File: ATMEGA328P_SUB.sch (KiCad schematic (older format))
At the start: 38 parts, among them J10 4/MISO, J11 5/SCK, J12 0, J13 1, J14 2, J15 ICSP1, J16 3, J17 4/SDA, J18 5/SCL, J19 0/RXD, J20 1/TXD, J21 2/INT0, J22 3/INT1, J23 4, J24 5, J25 6, J26 7, J27 5V, J28 3V3, J29 GND, J30 Vin, J4 AREF, J5 0, J6 1, J7 2, J8 7RO, J9 3/MOSI, SW1 RES, U6 ATmega328P-MU, Y2 16MHz

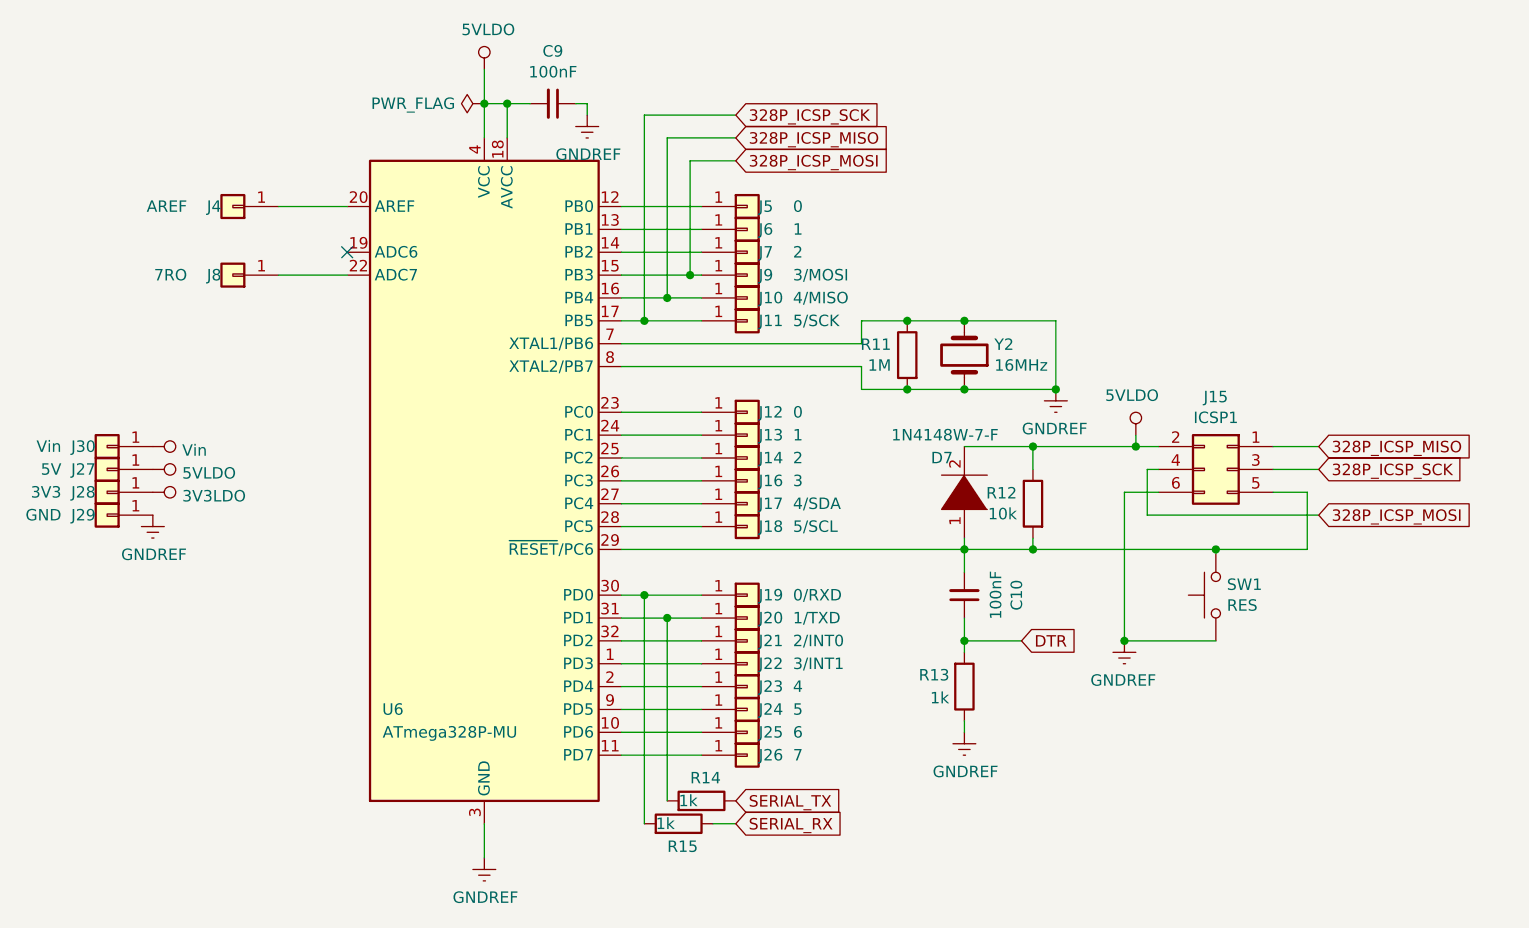
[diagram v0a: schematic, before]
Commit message: Set component footprints, added datasheets, fixed the last DRC error and a couple component values
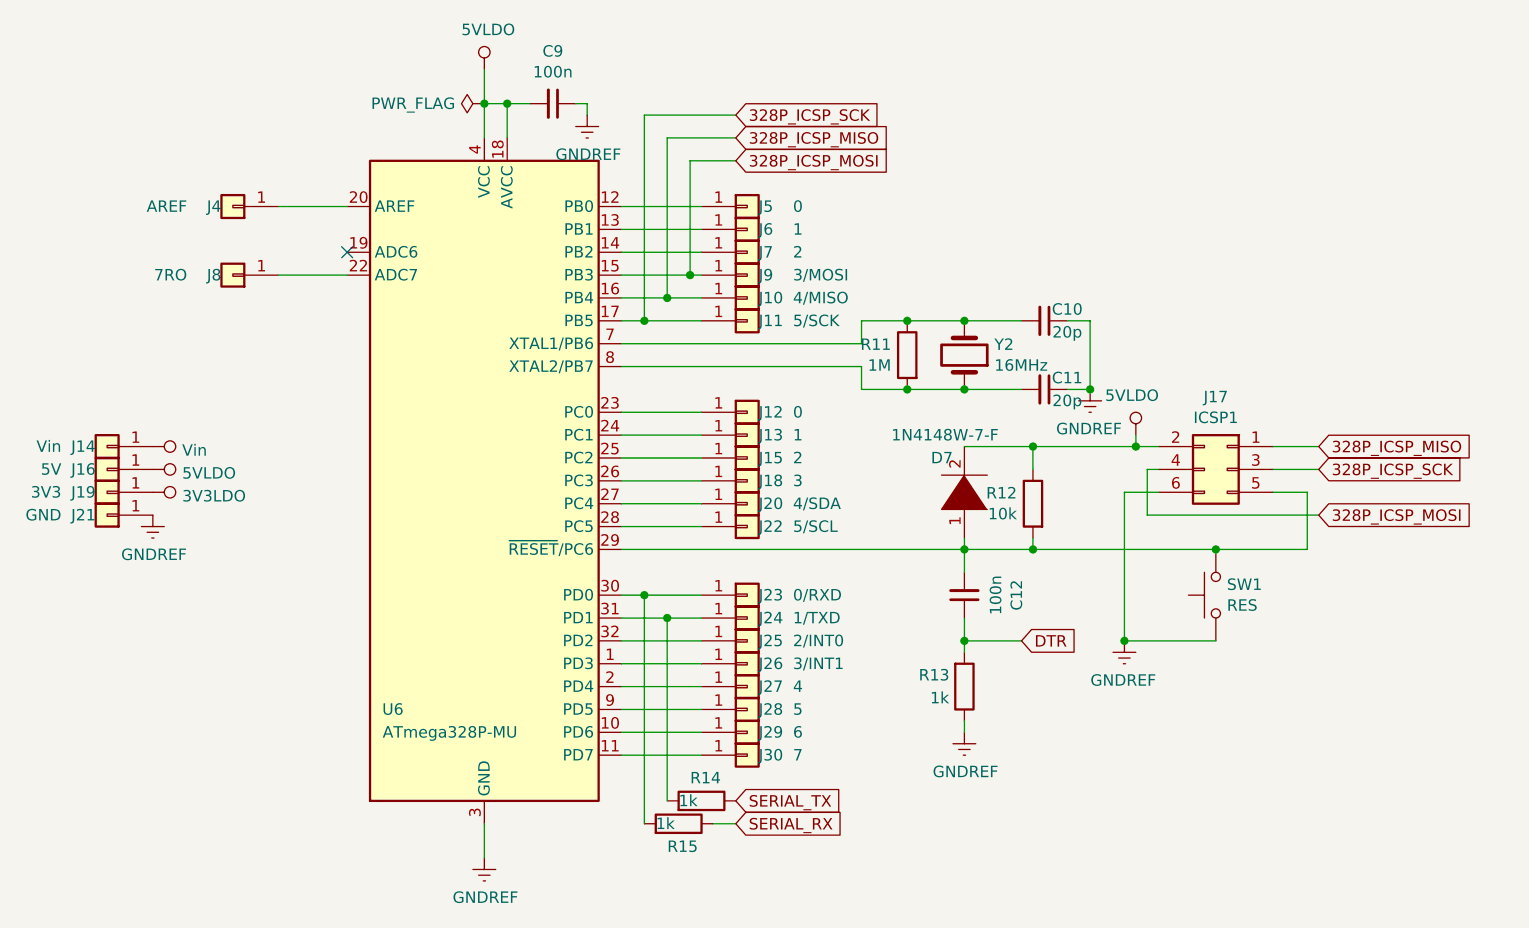
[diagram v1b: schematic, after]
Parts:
- added C10, C11: 20p, Capacitor_SMD:C_0603_1608Metric, symbol Device:C_Small
- C12: renamed from C10; value 100nF -> 100n; footprint (none) -> Capacitor_SMD:C_0603_1608Metric
- C9: value 100nF -> 100n; footprint (none) -> Capacitor_SMD:C_0603_1608Metric
- D7: footprint (none) -> Diode_SMD:D_SOD-123
- J10, J11, J12, J13, J4, J5, J6, J7, J8, J9: footprint (none) -> Connector_Pin:Pin_D1.0mm_L10.0mm
- J14: renamed from J30; footprint (none) -> Connector_Pin:Pin_D1.0mm_L10.0mm
- J15: renamed from J14; footprint (none) -> Connector_Pin:Pin_D1.0mm_L10.0mm
- J16: renamed from J27; footprint (none) -> Connector_Pin:Pin_D1.0mm_L10.0mm
- J17: renamed from J15; footprint (none) -> Connector_PinHeader_2.54mm:PinHeader_2x03_P2.54mm_Vertical
- J18: renamed from J16; footprint (none) -> Connector_Pin:Pin_D1.0mm_L10.0mm
- J19: renamed from J28; footprint (none) -> Connector_Pin:Pin_D1.0mm_L10.0mm
- J20: renamed from J17; footprint (none) -> Connector_Pin:Pin_D1.0mm_L10.0mm
- J21: renamed from J29; footprint (none) -> Connector_Pin:Pin_D1.0mm_L10.0mm
- J22: renamed from J18; footprint (none) -> Connector_Pin:Pin_D1.0mm_L10.0mm
- J23: renamed from J19; footprint (none) -> Connector_Pin:Pin_D1.0mm_L10.0mm
- J24: renamed from J20; footprint (none) -> Connector_Pin:Pin_D1.0mm_L10.0mm
- J25: renamed from J21; footprint (none) -> Connector_Pin:Pin_D1.0mm_L10.0mm
- J26: renamed from J22; footprint (none) -> Connector_Pin:Pin_D1.0mm_L10.0mm
- J27: renamed from J23; footprint (none) -> Connector_Pin:Pin_D1.0mm_L10.0mm
- J28: renamed from J24; footprint (none) -> Connector_Pin:Pin_D1.0mm_L10.0mm
- J29: renamed from J25; footprint (none) -> Connector_Pin:Pin_D1.0mm_L10.0mm
- J30: renamed from J26; footprint (none) -> Connector_Pin:Pin_D1.0mm_L10.0mm
- R11, R12, R13, R14, R15: footprint (none) -> Resistor_SMD:R_0603_1608Metric
- SW1: footprint (none) -> Button_Switch_SMD:SW_SPST_EVQP2
- Y2: footprint (none) -> Crystal:Crystal_SMD_SeikoEpson_MA505-2Pin_12.7x5.1mm
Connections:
- net GNDREF: now also C10.1, C11.1; no longer R11.1, R11.2, U6.7 (XTAL1/PB6), U6.8 (XTAL2/PB7), Y2.1, Y2.2
- new net: C10.2, R11.1, U6.7 (XTAL1/PB6), Y2.2
- new net: C11.2, R11.2, U6.8 (XTAL2/PB7), Y2.1

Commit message: Updated the schematic, added missing footprints, started PCB design
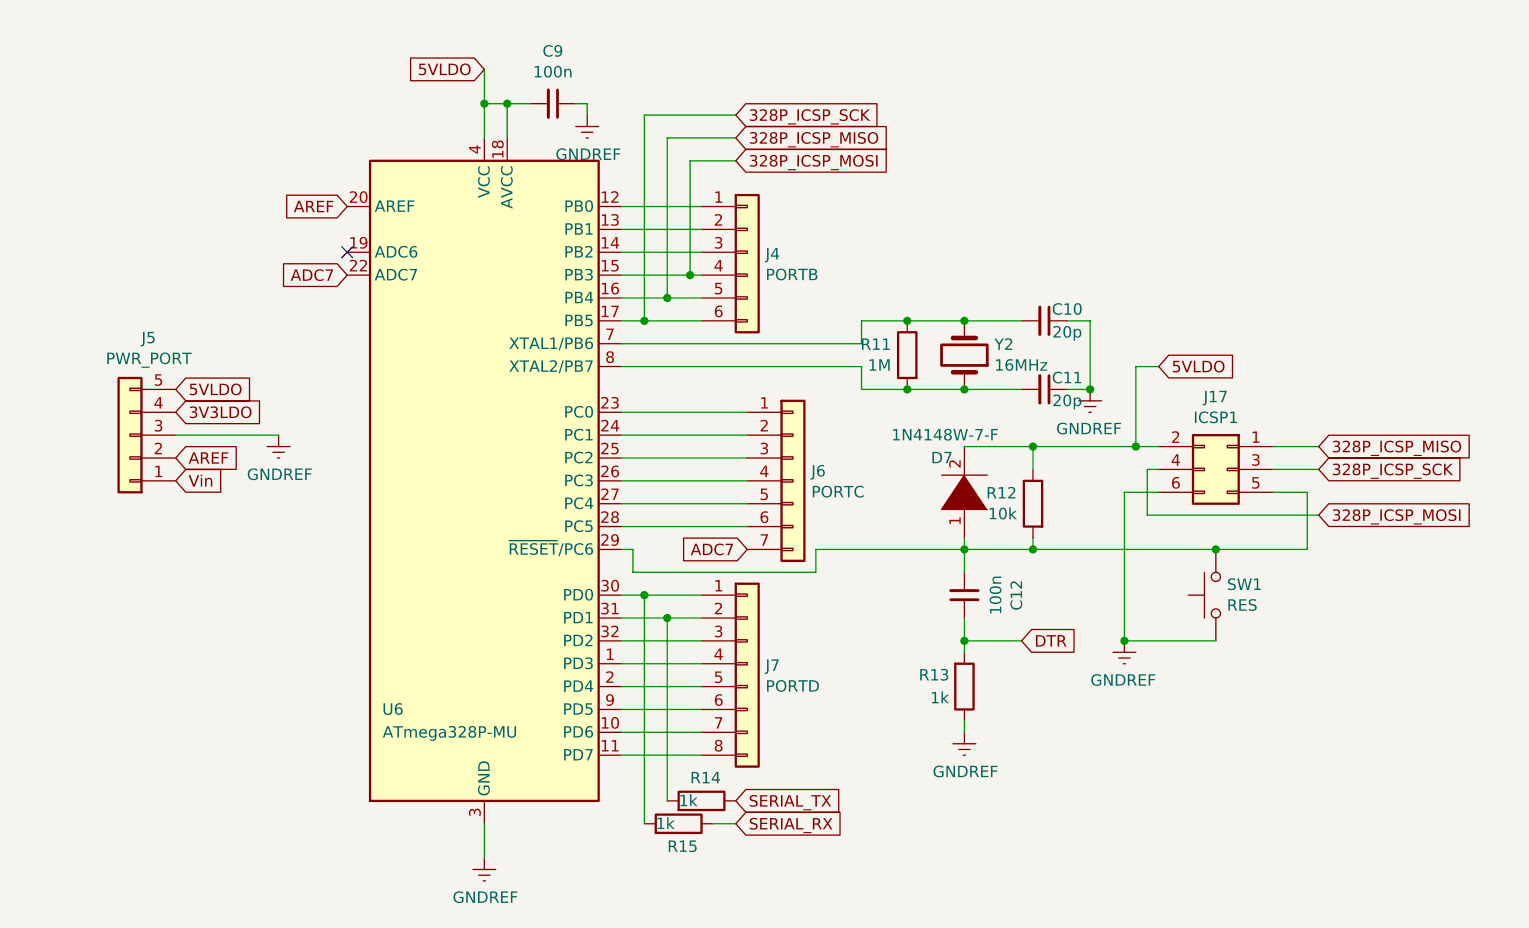
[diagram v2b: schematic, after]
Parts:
- removed J10: 4/MISO, Connector_Pin:Pin_D1.0mm_L10.0mm, symbol Connector_Generic:Conn_01x01
- removed J11: 5/SCK, Connector_Pin:Pin_D1.0mm_L10.0mm, symbol Connector_Generic:Conn_01x01
- removed J12, J5: 0, Connector_Pin:Pin_D1.0mm_L10.0mm, symbol Connector_Generic:Conn_01x01
- removed J13, J6: 1, Connector_Pin:Pin_D1.0mm_L10.0mm, symbol Connector_Generic:Conn_01x01
- removed J14: Vin, Connector_Pin:Pin_D1.0mm_L10.0mm, symbol Connector_Generic:Conn_01x01
- removed J15, J7: 2, Connector_Pin:Pin_D1.0mm_L10.0mm, symbol Connector_Generic:Conn_01x01
- removed J16: 5V, Connector_Pin:Pin_D1.0mm_L10.0mm, symbol Connector_Generic:Conn_01x01
- removed J18: 3, Connector_Pin:Pin_D1.0mm_L10.0mm, symbol Connector_Generic:Conn_01x01
- removed J19: 3V3, Connector_Pin:Pin_D1.0mm_L10.0mm, symbol Connector_Generic:Conn_01x01
- removed J20: 4/SDA, Connector_Pin:Pin_D1.0mm_L10.0mm, symbol Connector_Generic:Conn_01x01
- removed J21: GND, Connector_Pin:Pin_D1.0mm_L10.0mm, symbol Connector_Generic:Conn_01x01
- removed J22: 5/SCL, Connector_Pin:Pin_D1.0mm_L10.0mm, symbol Connector_Generic:Conn_01x01
- removed J23: 0/RXD, Connector_Pin:Pin_D1.0mm_L10.0mm, symbol Connector_Generic:Conn_01x01
- removed J24: 1/TXD, Connector_Pin:Pin_D1.0mm_L10.0mm, symbol Connector_Generic:Conn_01x01
- removed J25: 2/INT0, Connector_Pin:Pin_D1.0mm_L10.0mm, symbol Connector_Generic:Conn_01x01
- removed J26: 3/INT1, Connector_Pin:Pin_D1.0mm_L10.0mm, symbol Connector_Generic:Conn_01x01
- removed J27: 4, Connector_Pin:Pin_D1.0mm_L10.0mm, symbol Connector_Generic:Conn_01x01
- removed J28: 5, Connector_Pin:Pin_D1.0mm_L10.0mm, symbol Connector_Generic:Conn_01x01
- removed J29: 6, Connector_Pin:Pin_D1.0mm_L10.0mm, symbol Connector_Generic:Conn_01x01
- removed J30: 7, Connector_Pin:Pin_D1.0mm_L10.0mm, symbol Connector_Generic:Conn_01x01
- removed J4: AREF, Connector_Pin:Pin_D1.0mm_L10.0mm, symbol Connector_Generic:Conn_01x01
- removed J8: 7RO, Connector_Pin:Pin_D1.0mm_L10.0mm, symbol Connector_Generic:Conn_01x01
- removed J9: 3/MOSI, Connector_Pin:Pin_D1.0mm_L10.0mm, symbol Connector_Generic:Conn_01x01
- added J4: PORTB, Connector_PinHeader_2.54mm:PinHeader_1x06_P2.54mm_Vertical, symbol Connector_Generic:Conn_01x06
- added J5: PWR_PORT, Connector_PinHeader_2.54mm:PinHeader_1x05_P2.54mm_Vertical, symbol Connector_Generic:Conn_01x05
- added J6: PORTC, Connector_PinHeader_2.54mm:PinHeader_1x07_P2.54mm_Vertical, symbol Connector_Generic:Conn_01x07
- added J7: PORTD, Connector_PinHeader_2.54mm:PinHeader_1x08_P2.54mm_Vertical, symbol Connector_Generic:Conn_01x08
- Y2: footprint Crystal:Crystal_SMD_SeikoEpson_MA505-2Pin_12.7x5.1mm -> footprints:HC-49S
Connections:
- net 328P_ICSP_MISO: now also J4.5 (Pin_5)
- net 328P_ICSP_MOSI: now also J4.4 (Pin_4)
- net 328P_ICSP_SCK: now also J4.6 (Pin_6)
- net GNDREF: now also J5.3 (Pin_3)
- net 5VLDO: now reaches D7.2 (A), J17.2 (Pin_2), R12.1
- net 5VLDO: now also C9.2, U6.18 (AVCC), U6.4 (VCC), U6.6 (VCC), J5.5 (Pin_5)
- net at U6.1 (PD3): now also J7.4 (Pin_4)
- net at U6.10 (PD6): now also J7.7 (Pin_7)
- net at U6.11 (PD7): now also J7.8 (Pin_8)
- net at U6.12 (PB0): now also J4.1 (Pin_1)
- net at U6.13 (PB1): now also J4.2 (Pin_2)
- net at U6.14 (PB2): now also J4.3 (Pin_3)
- net at U6.2 (PD4): now also J7.5 (Pin_5)
- net AREF: now reaches U6.20 (AREF)
- net AREF: now also J5.2 (Pin_2)
- net ADC7: now reaches U6.22 (ADC7)
- net ADC7: now also J6.7 (Pin_7)
- net at U6.23 (PC0): now also J6.1 (Pin_1)
- net at U6.24 (PC1): now also J6.2 (Pin_2)
- net at U6.25 (PC2): now also J6.3 (Pin_3)
- net at U6.26 (PC3): now also J6.4 (Pin_4)
- net at U6.27 (PC4): now also J6.5 (Pin_5)
- net at U6.28 (PC5): now also J6.6 (Pin_6)
- net at R15.2, U6.30 (PD0): now also J7.1 (Pin_1)
- net at R14.2, U6.31 (PD1): now also J7.2 (Pin_2)
- net at U6.32 (PD2): now also J7.3 (Pin_3)
- net at U6.9 (PD5): now also J7.6 (Pin_6)
- new net 3V3LDO: J5.4 (Pin_4)
- new net Vin: J5.1 (Pin_1)
